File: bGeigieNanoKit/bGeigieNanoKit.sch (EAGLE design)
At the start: 36 parts, among them T1 2SC1815

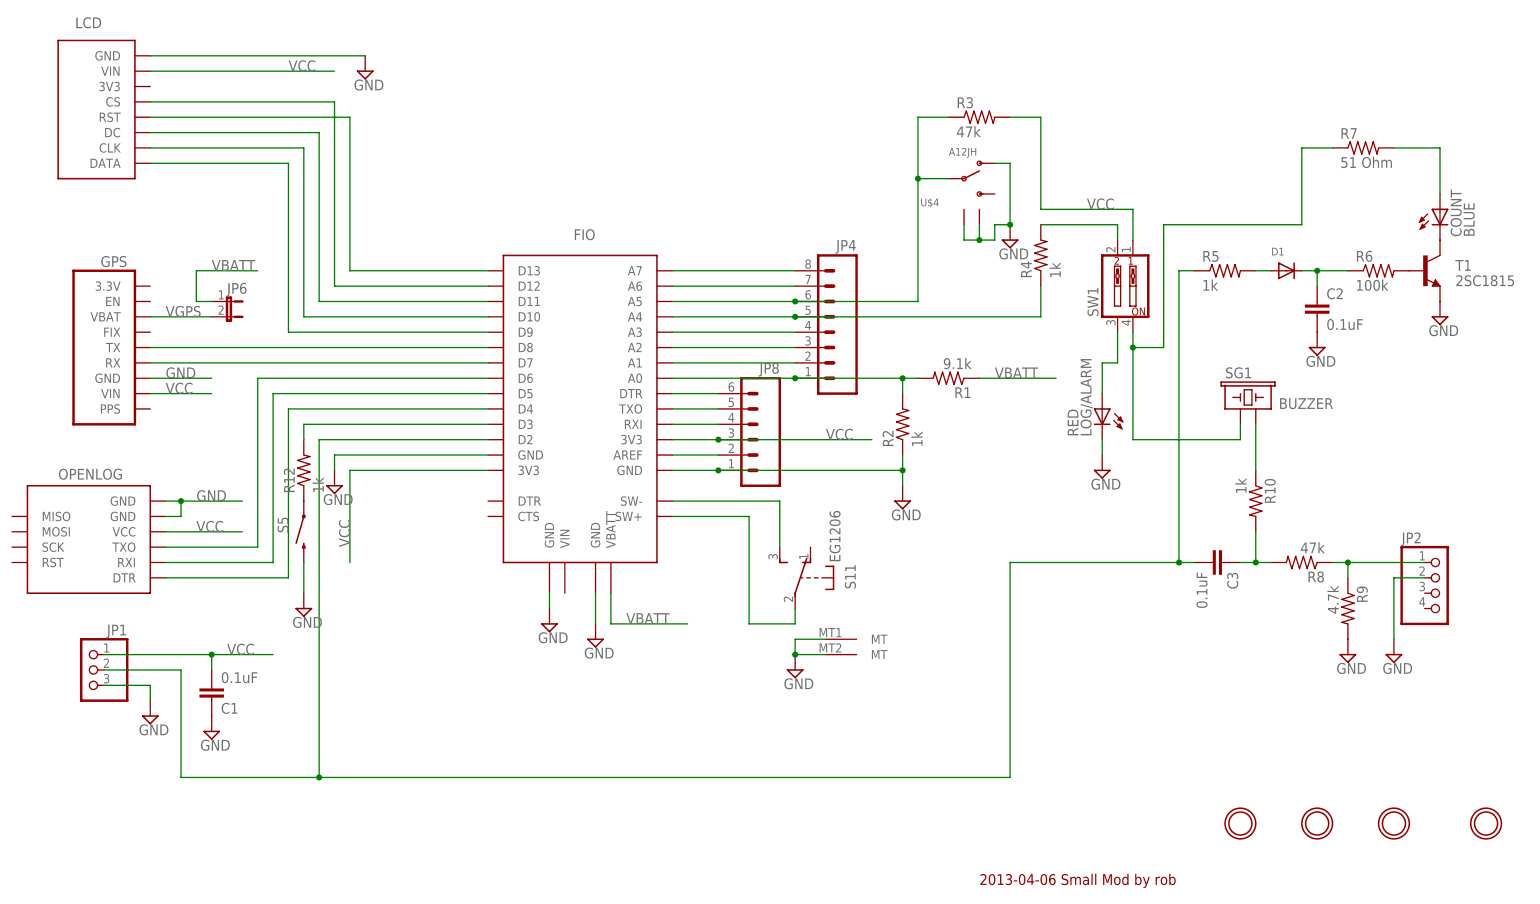
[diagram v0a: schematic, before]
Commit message: Revert "Changed R8 to 47k and and R9 to 4.7k and fixed some overlaying text."
This reverts commit f053eba477d0c686d0d0ac7e4f314e797ef1138b.
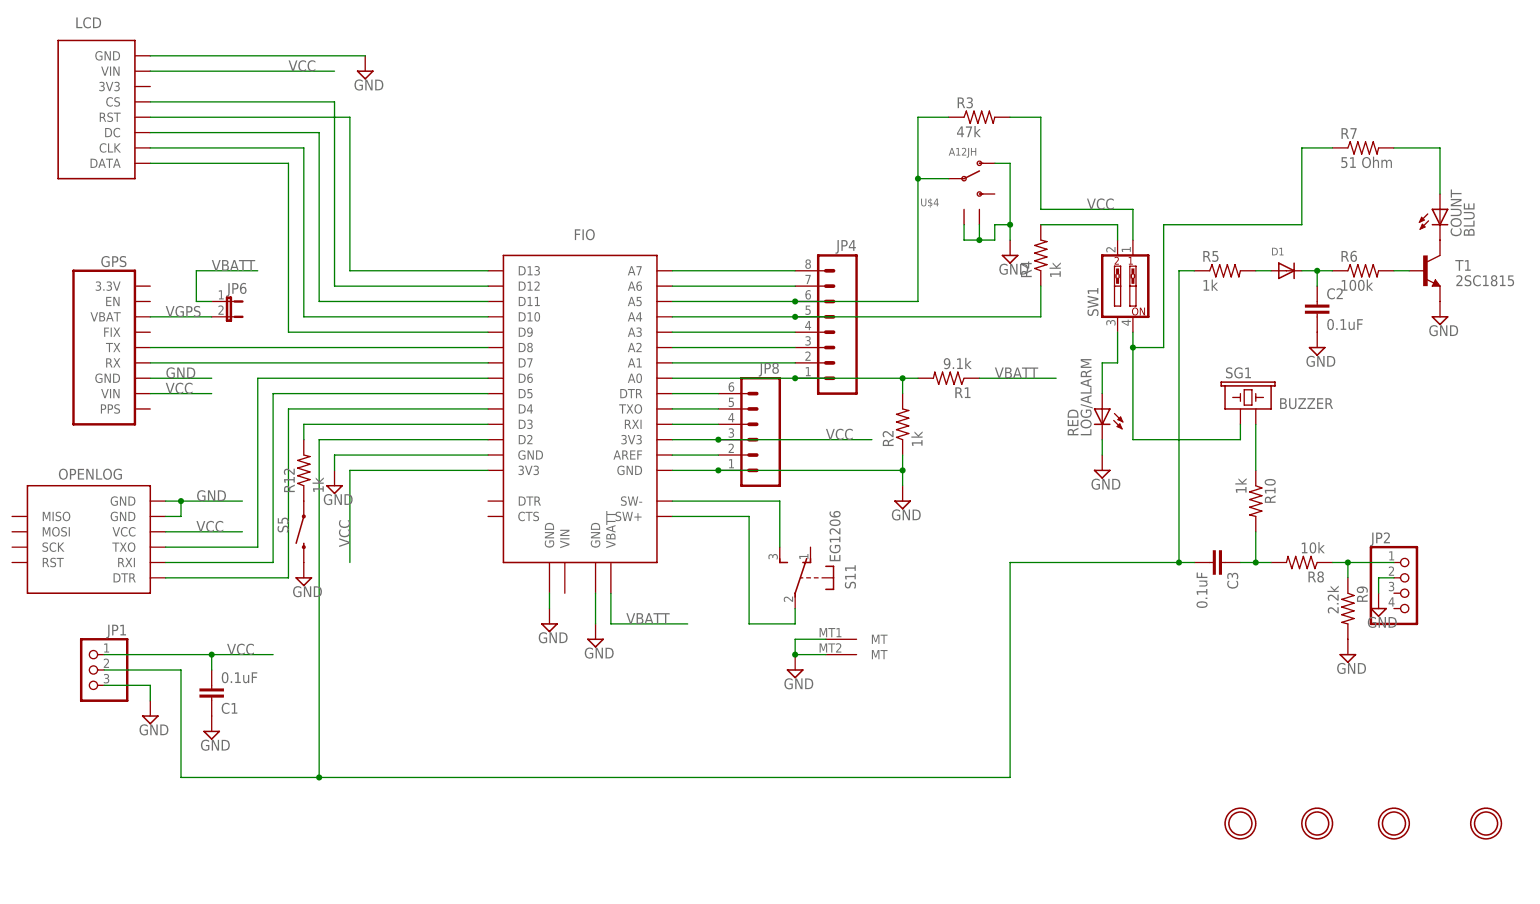
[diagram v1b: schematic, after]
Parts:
- R8: value 47k -> 10k
- R9: value 4.7k -> 2.2k
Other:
- note removed: "2013-04-06 Small Mod by rob"
- moved on the sheet: JP2, R6

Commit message: Changed R8 to 47k and and R9 to 4.7k and fixed some overlaying text.
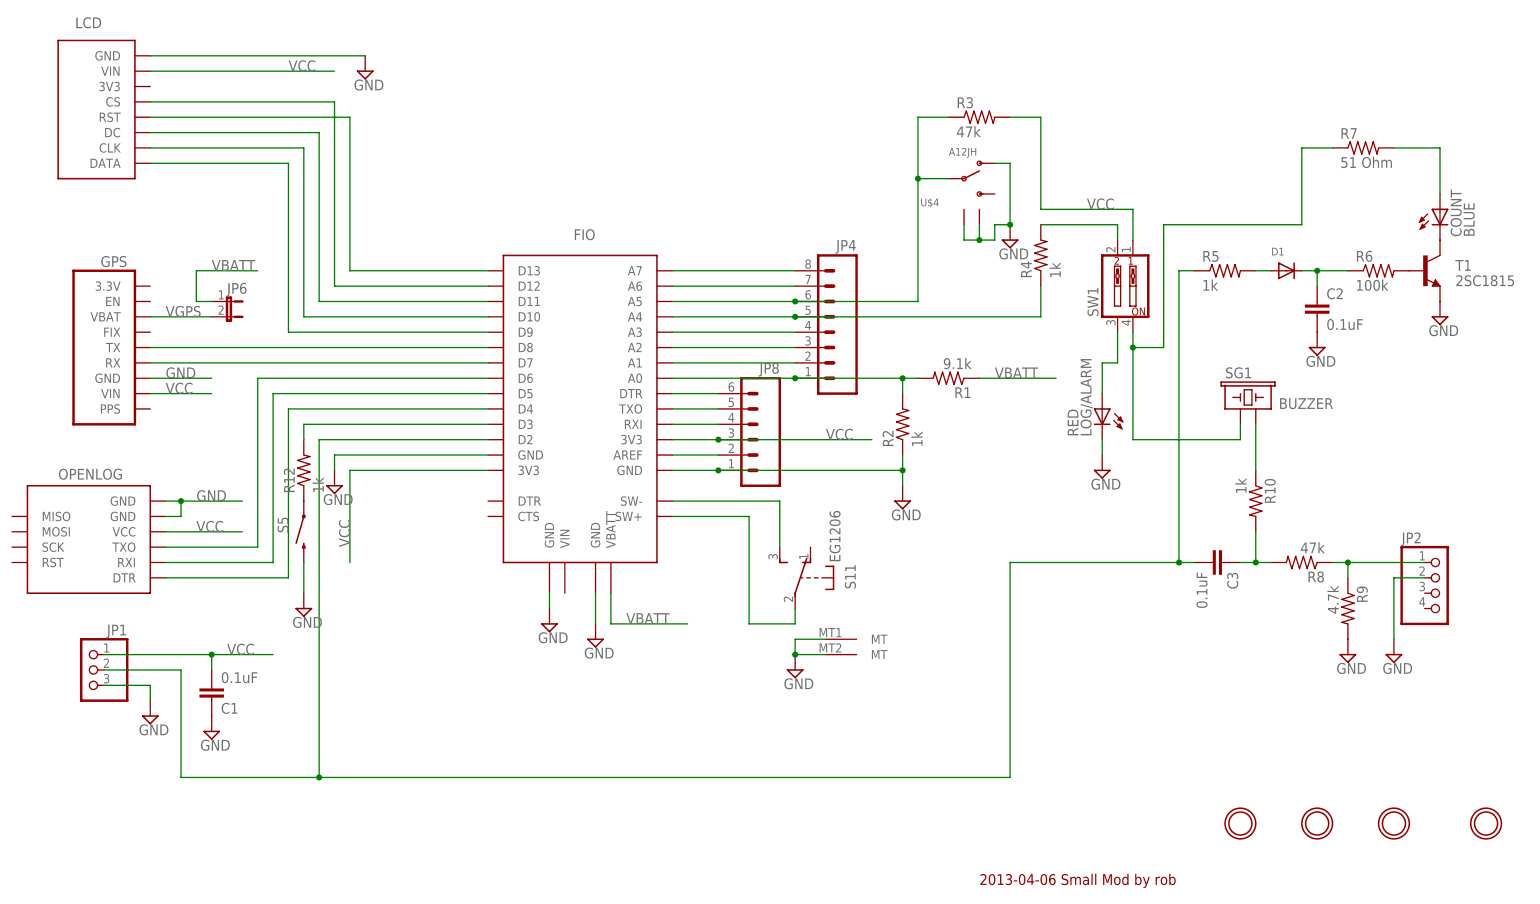
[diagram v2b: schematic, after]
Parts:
- R8: value 10k -> 47k
- R9: value 2.2k -> 4.7k
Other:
- note added: "2013-04-06 Small Mod by rob"
- moved on the sheet: JP2, R6
